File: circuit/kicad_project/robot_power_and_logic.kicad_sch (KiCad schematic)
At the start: 17 parts, among them J1 HC-05 connection socket, M1 Motor_DC, M2 Motor_DC, SW1 POWER, SW2 Reset, U1 LM7805_TO220, U2 Pico, U3 L293D, U4 L293D

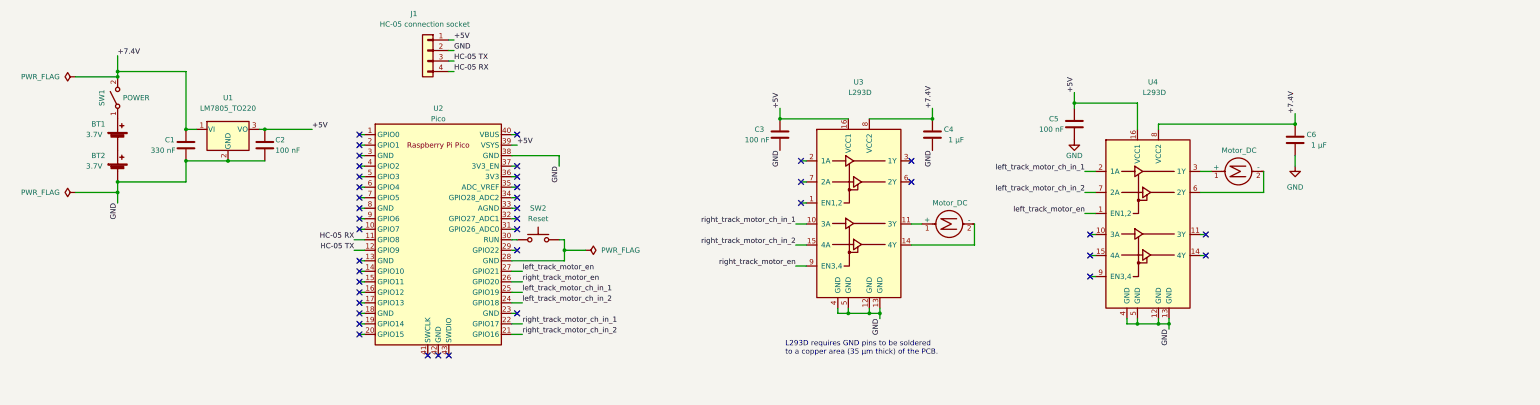
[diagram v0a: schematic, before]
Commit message: Add screw terminal
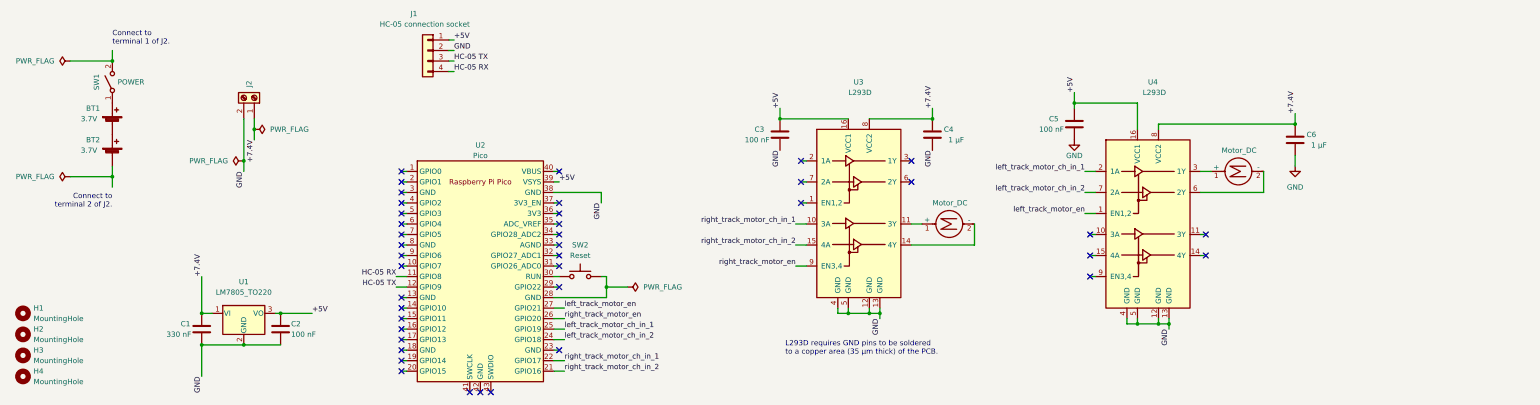
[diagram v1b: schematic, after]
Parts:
- added H1, H2, H3, H4: MountingHole, symbol Mechanical:MountingHole
- added J2: Screw_Terminal_01x02, symbol Connector:Screw_Terminal_01x02
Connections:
- net +7.4V: now also J2.1 (Pin_1); no longer SW1.2 (B)
- net GND: now also J2.2 (Pin_2); no longer BT2.2 (-)
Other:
- note added: "Connect to terminal 1 of J2."
- note added: "Connect to terminal 2 of J2."
- moved on the sheet: BT1, BT2, C1, C2, SW1, SW2, U1, U2

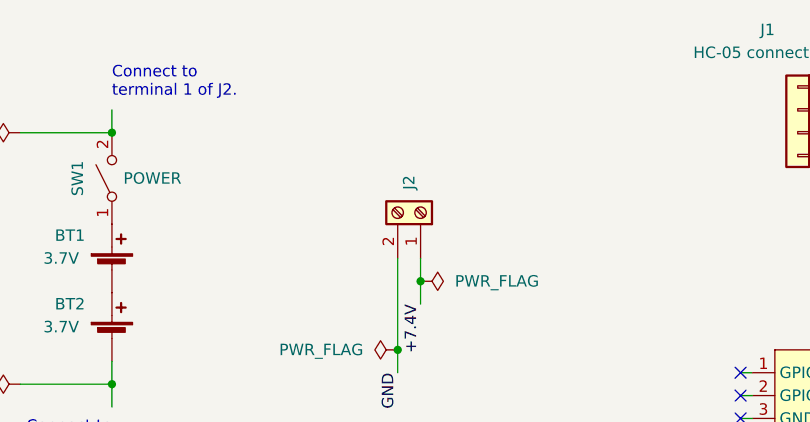
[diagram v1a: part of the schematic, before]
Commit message: Add mounting holes and swap pins of screw terminal
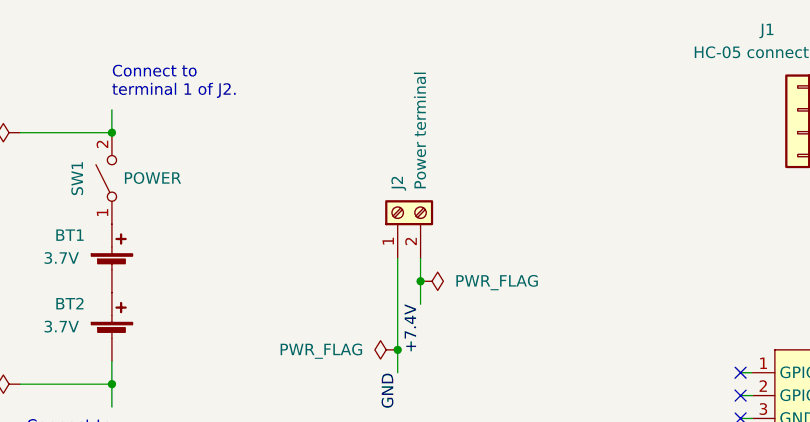
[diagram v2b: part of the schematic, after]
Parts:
- H1, H2, H3, H4: footprint (none) -> MountingHole:MountingHole_3.2mm_M3
- J2: value Screw_Terminal_01x02 -> Power terminal; footprint (none) -> TerminalBlock_Phoenix:TerminalBlock_Phoenix_MPT-0,5-2-2.54_1x02_P2.54mm_Horizontal
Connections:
- net +7.4V: now also J2.2 (Pin_2); no longer J2.1 (Pin_1)
- net GND: now also J2.1 (Pin_1); no longer J2.2 (Pin_2)
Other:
- moved on the sheet: J2

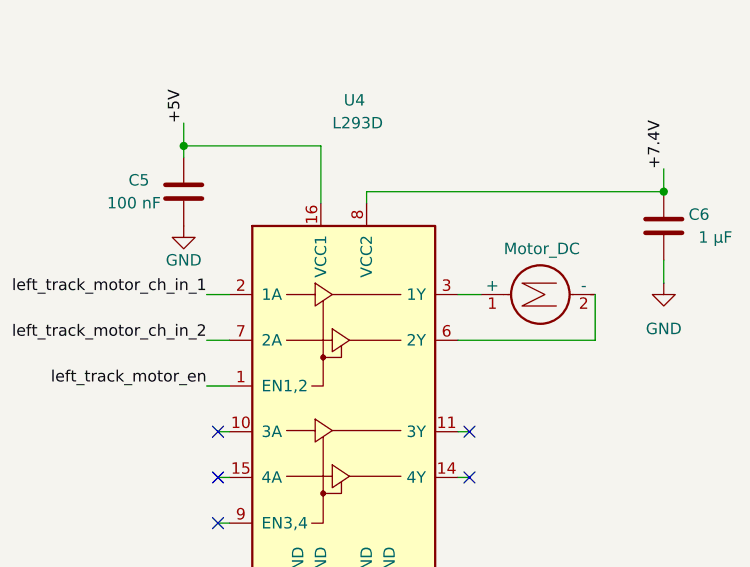
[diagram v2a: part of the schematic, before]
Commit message: Replace some GND symbols with GND labels
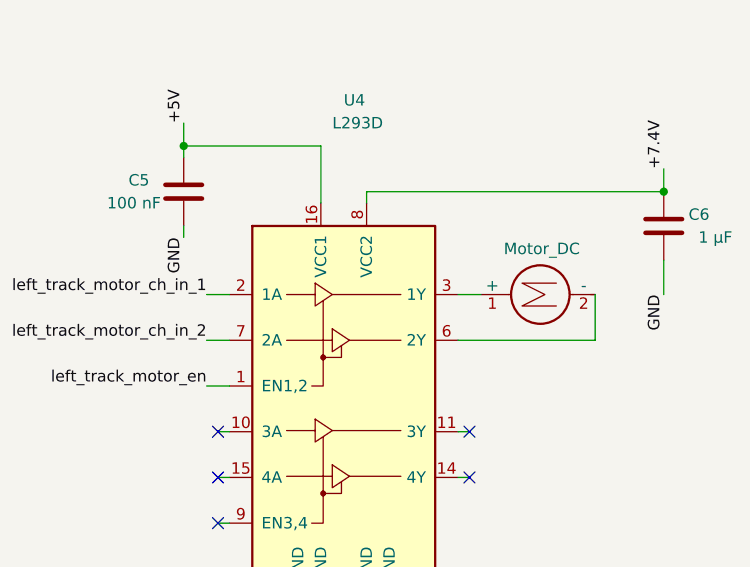
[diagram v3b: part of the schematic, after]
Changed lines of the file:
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@@
-    (stroke (width 0) (type default) (color 0 0 0 0))
-  )
-  (wire (pts (xy 327.66 54.61) (xy 327.66 52.07))
     (stroke (width 0) (type default) (color 0 0 0 0))
   )
@@
     (stroke (width 0) (type default) (color 0 0 0 0))
   )
+  (wire (pts (xy 327.66 55.88) (xy 327.66 52.07))
+    (stroke (width 0) (type default) (color 0 0 0 0))
+  )
   (wire (pts (xy 41.91 57.15) (xy 41.91 54.61))
     (stroke (width 0) (type default) (color 0 0 0 0))
@@
   )
   (wire (pts (xy 149.86 81.28) (xy 148.59 81.28))
+    (stroke (width 0) (type default) (color 0 0 0 0))
+  )
+  (wire (pts (xy 274.32 49.53) (xy 274.32 48.26))
     (stroke (width 0) (type default) (color 0 0 0 0))
   )
@@
     (effects (font (size 1.27 1.27)) (justify right bottom))
   )
+  (label "GND" (at 327.66 55.88 270)
+    (effects (font (size 1.27 1.27)) (justify right bottom))
+  )
   (label "GND" (at 160.02 63.5 270)
     (effects (font (size 1.27 1.27)) (justify right bottom))
@@
   (label "right_track_motor_en" (at 151.13 91.44 0)
     (effects (font (size 1.27 1.27)) (justify left bottom))
+  )
+  (label "GND" (at 274.32 49.53 270)
+    (effects (font (size 1.27 1.27)) (justify right bottom))
   )
   (label "HC-05 RX" (at 124.46 31.75 0)
@@
     (pin "1")
     (pin "2")
-  )
-  (symbol (lib_id "power:GND") (at 274.32 48.26 0) (unit 1)
-    (in_bom yes) (on_board yes)
-    (property "Reference" "#PWR05" (id 0) (at 274.32 54.61 0)
-      (effects (font (size 1.27 1.27)) hide)
-    )
-    (property "Value" "GND" (id 1) (at 274.32 52.07 0))
-    (property "Footprint" "" (id 2) (at 274.32 48.26 0)
-      (effects (font (size 1.27 1.27)) hide)
-    )
-    (property "Datasheet" "" (id 3) (at 274.32 48.26 0)
-      (effects (font (size 1.27 1.27)) hide)
-    )
-    (pin "1")
   )
   (symbol (lib_id "power:PWR_FLAG") (at 76.2 45.72 270) (mirror x) (unit 1)
@@
     )
   )
-  (symbol (lib_id "power:GND") (at 327.66 54.61 0) (unit 1)
-    (in_bom yes) (on_board yes) (fields_autoplaced)
-    (property "Reference" "#PWR07" (id 0) (at 327.66 60.96 0)
-      (effects (font (size 1.27 1.27)) hide)
-    )
-    (property "Value" "GND" (id 1) (at 327.66 59.69 0))
-    (property "Footprint" "" (id 2) (at 327.66 54.61 0)
-      (effects (font (size 1.27 1.27)) hide)
-    )
-    (property "Datasheet" "" (id 3) (at 327.66 54.61 0)
-      (effects (font (size 1.27 1.27)) hide)
-    )
-    (pin "1")
-  )
   (symbol (lib_id "Device:C") (at 240.03 46.99 180) (unit 1)
     (in_bom yes) (on_board yes)
@@
       (reference "#FLG05") (unit 1) (value "PWR_FLAG") (footprint "")
     )
-    (path "/33e34b48-3ca1-4bb5-9ed0-309643124671"
-      (reference "#PWR05") (unit 1) (value "GND") (footprint "")
-    )
-    (path "/e6f31215-ae32-4caa-ac55-0d100ae1aacb"
-      (reference "#PWR07") (unit 1) (value "GND") (footprint "")
-    )
     (path "/8f2c1bec-796b-4d34-8b1e-e772b4921583"

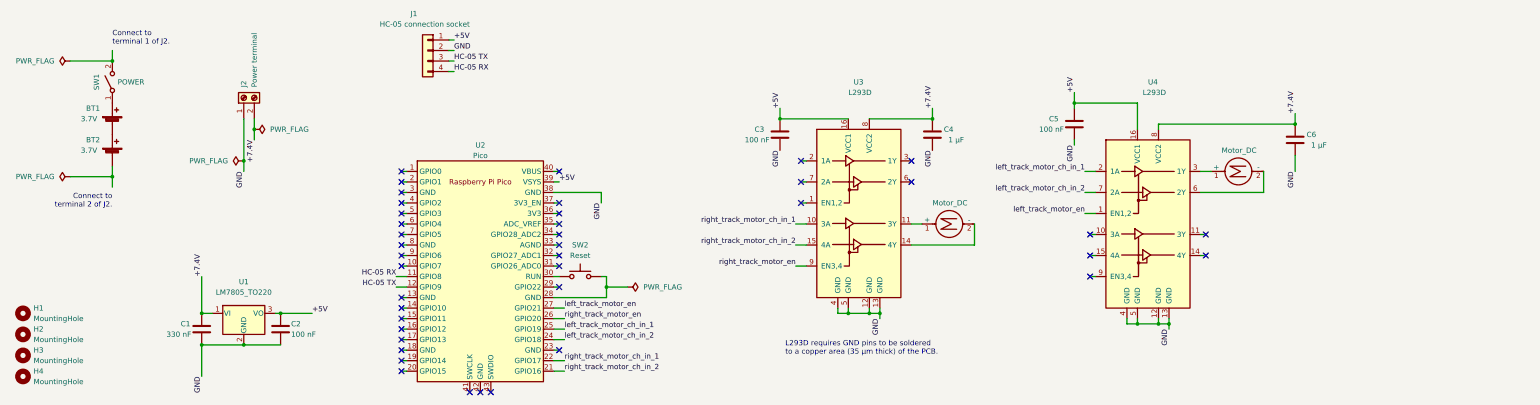
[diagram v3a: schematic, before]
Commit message: Replace motors with their connection sockets
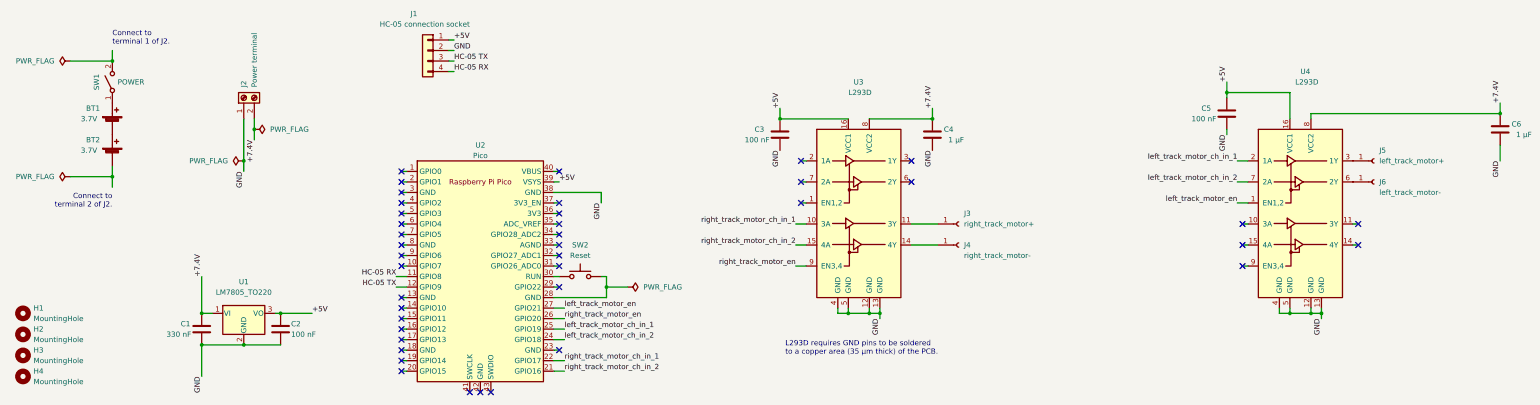
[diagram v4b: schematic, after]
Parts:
- removed M1, M2: Motor_DC, symbol Motor:Motor_DC
- added J3: right_track_motor+, Connector_PinSocket_2.54mm:PinSocket_1x01_P2.54mm_Vertical, symbol Connector:Conn_01x01_Female
- added J4: right_track_motor-, Connector_PinSocket_2.54mm:PinSocket_1x01_P2.54mm_Vertical, symbol Connector:Conn_01x01_Female
- added J5: left_track_motor+, Connector_PinSocket_2.54mm:PinSocket_1x01_P2.54mm_Vertical, symbol Connector:Conn_01x01_Female
- added J6: left_track_motor-, Connector_PinSocket_2.54mm:PinSocket_1x01_P2.54mm_Vertical, symbol Connector:Conn_01x01_Female
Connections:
- net at U4.3 (1Y): now also J5.1 (Pin_1)
- net at U4.6 (2Y): now also J6.1 (Pin_1)
- net at U3.11 (3Y): now also J3.1 (Pin_1)
- net at U3.14 (4Y): now also J4.1 (Pin_1)
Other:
- moved on the sheet: C5, C6, U4
